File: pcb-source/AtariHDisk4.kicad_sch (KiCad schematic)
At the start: 19 parts, among them J1 JTAG, U4 Oscillator7x5, U9 5M80Z

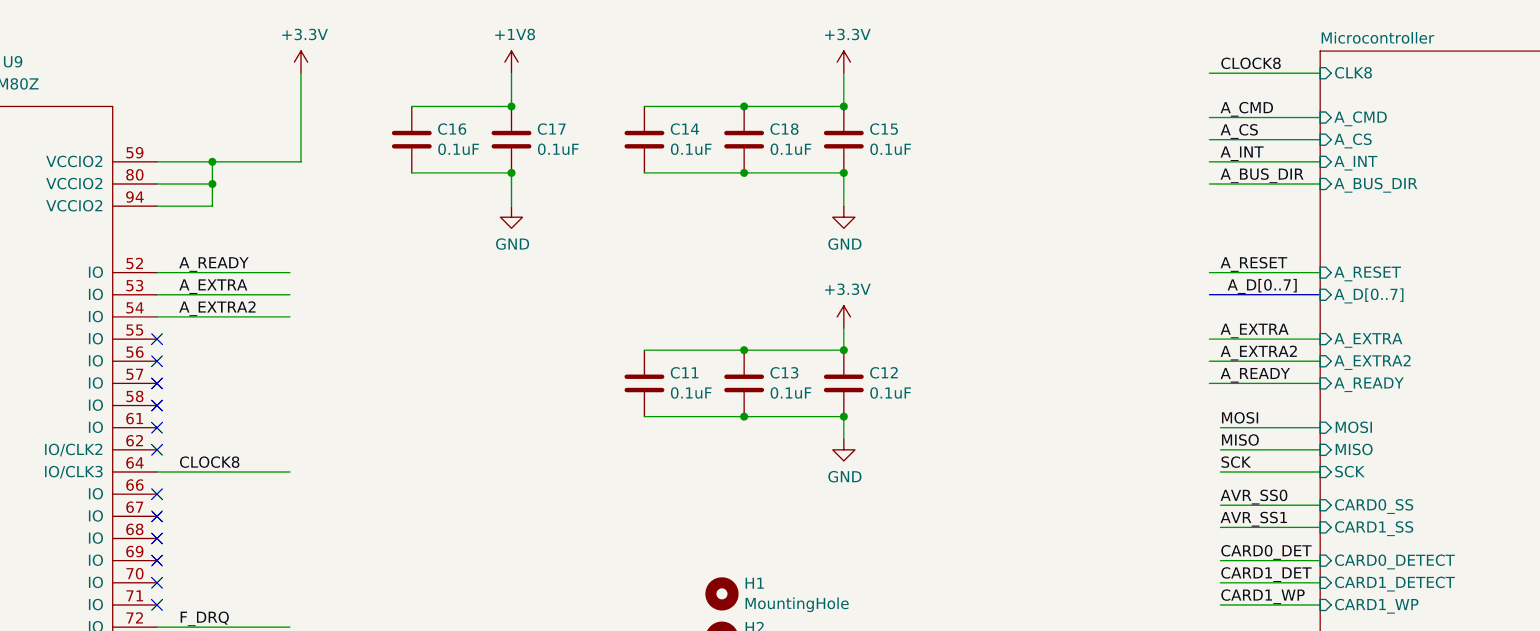
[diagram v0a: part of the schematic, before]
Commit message: Switched the avr128da to an stm32c031
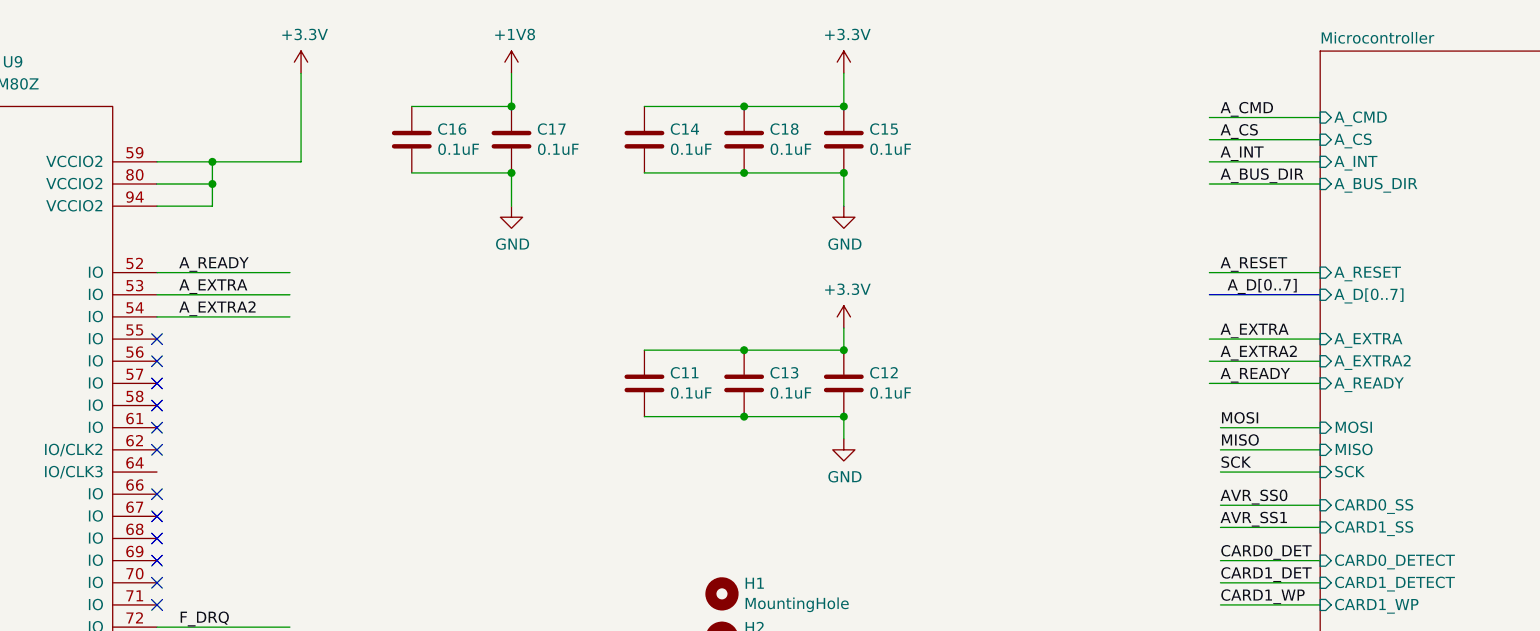
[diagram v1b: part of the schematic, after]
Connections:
- net CLOCK8: no longer names the net of U9.64 (IO/CLK3)
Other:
- sheet Microcontroller ports: added none; removed CLK8
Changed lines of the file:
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@@
-    (stroke (width 0) (type default))
-  )
-  (wire (pts (xy 104.14 73.66) (xy 119.38 73.66))
     (stroke (width 0) (type default))
   )
@@
     (stroke (width 0) (type default))
   )
-  (wire (pts (xy 224.79 27.94) (xy 237.49 27.94))
-    (stroke (width 0) (type default))
-  )
   (wire (pts (xy 104.14 147.32) (xy 119.38 147.32))
     (stroke (width 0) (type default))
@@
   )
   (label "A_READY" (at 226.06 63.5 0) (fields_autoplaced)
-    (effects (font (size 1.27 1.27)) (justify left bottom))
-  )
-  (label "CLOCK8" (at 226.06 27.94 0) (fields_autoplaced)
     (effects (font (size 1.27 1.27)) (justify left bottom))
   )
@@
   )
   (label "F_D[0..7]" (at 242.57 114.3 0) (fields_autoplaced)
-    (effects (font (size 1.27 1.27)) (justify left bottom))
-  )
-  (label "CLOCK8" (at 106.68 73.66 0) (fields_autoplaced)
     (effects (font (size 1.27 1.27)) (justify left bottom))
   )
@@
       (effects (font (size 1.27 1.27)) (justify left))
     )
-    (pin "CLK8" input (at 237.49 27.94 180)
-      (effects (font (size 1.27 1.27)) (justify left))
-    )

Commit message: Final board setup that was sent to production
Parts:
- added JP1: SolderJumper_2_Open, Jumper:SolderJumper-2_P1.3mm_Open_RoundedPad1.0x1.5mm, symbol Jumper:SolderJumper_2_Open
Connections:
- net A_BUS_DIR: now also U9.29 (IO); no longer U9.49 (IO)
- net A_CMD: now also U9.28 (IO); no longer U9.50 (IO)
- net A_CS: now also U9.34 (IO); no longer U9.48 (IO)
- net A_EXTRA: now also U9.26 (IO); no longer U9.53 (IO)
- net A_EXTRA2: now also U9.27 (IO); no longer U9.54 (IO)
- net A_INT: now also U9.49 (IO); no longer U9.51 (IO)
- net A_READY: now also U9.50 (IO); no longer U9.52 (IO)
- net CLK32: now also JP1.2 (B)
- net A_RESET: no longer names the net of U9.33 (IO)
- new net A_CLKOUT: JP1.1 (A)
- no-connect marks 49 -> 51
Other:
- sheet Microcontroller ports: added CLKOUT; removed none
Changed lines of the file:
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@@
   (no_connect (at 104.14 124.46))
   (no_connect (at 71.12 101.6))
+  (no_connect (at 104.14 55.88))
   (no_connect (at 104.14 119.38))
   (no_connect (at 104.14 60.96))
-  (no_connect (at 71.12 93.98))
+  (no_connect (at 71.12 104.14))
+  (no_connect (at 71.12 137.16))
   (no_connect (at 104.14 127))
   (no_connect (at 71.12 81.28))
   (no_connect (at 35.56 180.34))
+  (no_connect (at 104.14 58.42))
   (no_connect (at 104.14 83.82))
+  (no_connect (at 104.14 73.66))
   (no_connect (at 104.14 111.76))
   (no_connect (at 71.12 78.74))
-  (no_connect (at 104.14 58.42))
-  (no_connect (at 71.12 99.06))
   (no_connect (at 104.14 109.22))
   (no_connect (at 104.14 81.28))
   (no_connect (at 189.23 147.32))
   (no_connect (at 104.14 132.08))
-  (no_connect (at 71.12 96.52))
+  (no_connect (at 71.12 144.78))
   (no_connect (at 104.14 137.16))
   (no_connect (at 104.14 88.9))
   (no_connect (at 71.12 73.66))
+  (no_connect (at 104.14 53.34))
   (no_connect (at 104.14 78.74))
   (no_connect (at 104.14 76.2))
-  (no_connect (at 71.12 91.44))
   (no_connect (at 104.14 71.12))
-  (no_connect (at 71.12 106.68))
   (no_connect (at 71.12 134.62))
   (no_connect (at 104.14 134.62))
@@
   (no_connect (at 71.12 63.5))
   (no_connect (at 71.12 68.58))
+  (no_connect (at 104.14 50.8))
   (bus_entry (at 55.88 114.3) (size -2.54 2.54)
     (stroke (width 0) (type default))
@@
     (stroke (width 0) (type default))
   )
+  (wire (pts (xy 224.79 27.94) (xy 237.49 27.94))
+    (stroke (width 0) (type default))
+  )
   (bus (pts (xy 53.34 50.8) (xy 53.34 48.26))
     (stroke (width 0) (type default))
@@
     (stroke (width 0) (type default))
   )
-  (wire (pts (xy 104.14 50.8) (xy 119.38 50.8))
-    (stroke (width 0) (type default))
-  )
   (wire (pts (xy 180.34 156.21) (xy 226.06 156.21))
     (stroke (width 0) (type default))
@@
     (stroke (width 0) (type default))
   )
-  (wire (pts (xy 104.14 55.88) (xy 119.38 55.88))
-    (stroke (width 0) (type default))
-  )
   (wire (pts (xy 241.3 105.41) (xy 257.81 105.41))
     (stroke (width 0) (type default))
@@
     (stroke (width 0) (type default))
   )
+  (wire (pts (xy 55.88 93.98) (xy 71.12 93.98))
+    (stroke (width 0) (type default))
+  )
   (wire (pts (xy 104.14 165.1) (xy 110.49 165.1))
     (stroke (width 0) (type default))
@@
     (stroke (width 0) (type default))
   )
+  (wire (pts (xy 55.88 106.68) (xy 71.12 106.68))
+    (stroke (width 0) (type default))
+  )
   (bus (pts (xy 121.92 154.94) (xy 143.51 154.94))
     (stroke (width 0) (type default))
@@
     (stroke (width 0) (type default))
   )
+  (wire (pts (xy 55.88 91.44) (xy 71.12 91.44))
+    (stroke (width 0) (type default))
+  )
   (wire (pts (xy 35.56 175.26) (xy 35.56 177.8))
     (stroke (width 0) (type default))
@@
     (stroke (width 0) (type default))
   )
-  (wire (pts (xy 55.88 104.14) (xy 71.12 104.14))
-    (stroke (width 0) (type default))
-  )
   (wire (pts (xy 177.8 142.24) (xy 177.8 128.27))
     (stroke (width 0) (type default))
@@
     (stroke (width 0) (type default))
   )
+  (wire (pts (xy 55.88 99.06) (xy 71.12 99.06))
+    (stroke (width 0) (type default))
+  )
   (wire (pts (xy 241.3 102.87) (xy 257.81 102.87))
     (stroke (width 0) (type default))
@@
     (stroke (width 0) (type default))
   )
-  (wire (pts (xy 55.88 137.16) (xy 71.12 137.16))
-    (stroke (width 0) (type default))
-  )
   (wire (pts (xy 201.93 139.7) (xy 208.28 139.7))
     (stroke (width 0) (type default))
@@
     (stroke (width 0) (type default))
   )
+  (wire (pts (xy 33.02 71.12) (xy 48.26 71.12))
+    (stroke (width 0) (type default))
+  )
   (bus (pts (xy 121.92 142.24) (xy 121.92 144.78))
     (stroke (width 0) (type default))
@@
     (stroke (width 0) (type default))
   )
-  (wire (pts (xy 104.14 53.34) (xy 119.38 53.34))
-    (stroke (width 0) (type default))
-  )
   (wire (pts (xy 63.5 40.64) (xy 63.5 38.1))
     (stroke (width 0) (type default))
@@
     (stroke (width 0) (type default))
   )
+  (wire (pts (xy 55.88 96.52) (xy 71.12 96.52))
+    (stroke (width 0) (type default))
+  )
   (wire (pts (xy 182.88 43.18) (xy 182.88 39.37))
     (stroke (width 0) (type default))
@@
     (stroke (width 0) (type default))
   )
-  (wire (pts (xy 55.88 144.78) (xy 71.12 144.78))
-    (stroke (width 0) (type default))
-  )
   (wire (pts (xy 237.49 60.96) (xy 224.79 60.96))
     (stroke (width 0) (type default))
@@
     (effects (font (size 1.27 1.27)) (justify left bottom))
   )
-  (label "A_READY" (at 106.68 50.8 0) (fields_autoplaced)
+  (label "A_READY" (at 57.15 142.24 0) (fields_autoplaced)
     (effects (font (size 1.27 1.27)) (justify left bottom))
   )
@@
     (effects (font (size 1.27 1.27)) (justify left bottom))
   )
-  (label "A_EXTRA" (at 106.68 53.34 0) (fields_autoplaced)
+  (label "A_EXTRA" (at 57.15 91.44 0) (fields_autoplaced)
     (effects (font (size 1.27 1.27)) (justify left bottom))
   )
@@
     (effects (font (size 1.27 1.27)) (justify left bottom))
   )
-  (label "A_BUS_DIR" (at 57.15 139.7 0) (fields_autoplaced)
+  (label "A_BUS_DIR" (at 57.15 99.06 0) (fields_autoplaced)
     (effects (font (size 1.27 1.27)) (justify left bottom))
   )
@@
     (effects (font (size 1.27 1.27)) (justify left bottom))
   )
-  (label "A_RESET" (at 57.15 104.14 0) (fields_autoplaced)
-    (effects (font (size 1.27 1.27)) (justify left bottom))
-  )
   (label "TD0" (at 218.44 128.27 0) (fields_autoplaced)
     (effects (font (size 1.27 1.27)) (justify left bottom))
@@
     (effects (font (size 1.27 1.27)) (justify left bottom))
   )
-  (label "A_CMD" (at 57.15 142.24 0) (fields_autoplaced)
+  (label "A_CMD" (at 57.15 96.52 0) (fields_autoplaced)
     (effects (font (size 1.27 1.27)) (justify left bottom))
   )
@@
     (effects (font (size 1.27 1.27)) (justify left bottom))
   )
-  (label "A_INT" (at 57.15 144.78 0) (fields_autoplaced)
+  (label "A_INT" (at 57.15 139.7 0) (fields_autoplaced)
     (effects (font (size 1.27 1.27)) (justify left bottom))
   )
@@
     (effects (font (size 1.27 1.27)) (justify left bottom))
   )
-  (label "A_CS" (at 57.15 137.16 0) (fields_autoplaced)
+  (label "A_CS" (at 57.15 106.68 0) (fields_autoplaced)
     (effects (font (size 1.27 1.27)) (justify left bottom))
   )
@@
     (effects (font (size 1.27 1.27)) (justify left bottom))
   )
-  (label "A_RESET" (at 226.06 50.8 0) (fields_autoplaced)
+  (label "F_RESET" (at 226.06 50.8 0) (fields_autoplaced)
     (effects (font (size 1.27 1.27)) (justify left bottom))
   )
@@
     (effects (font (size 1.27 1.27)) (justify left bottom))
   )
+  (label "A_CLKOUT" (at 34.29 71.12 0) (fields_autoplaced)
+    (effects (font (size 1.27 1.27)) (justify left bottom))
+  )
   (label "F_D4" (at 106.68 149.86 0) (fields_autoplaced)
     (effects (font (size 1.27 1.27)) (justify left bottom))
@@
     (effects (font (size 1.27 1.27)) (justify right bottom))
   )
-  (label "A_EXTRA2" (at 106.68 55.88 0) (fields_autoplaced)
+  (label "A_EXTRA2" (at 57.15 93.98 0) (fields_autoplaced)
     (effects (font (size 1.27 1.27)) (justify left bottom))
   )
@@
   )
   (label "A_EXTRA2" (at 226.06 60.96 0) (fields_autoplaced)
+    (effects (font (size 1.27 1.27)) (justify left bottom))
+  )
+  (label "A_CLKOUT" (at 226.06 27.94 0) (fields_autoplaced)
     (effects (font (size 1.27 1.27)) (justify left bottom))
   )
@@
         (path "/b85bd53e-a419-4638-ac5c-9132c68f9083"
           (reference "#PWR057") (unit 1)
+        )
+      )
+    )
+  )
+  (symbol (lib_id "Jumper:SolderJumper_2_Open") (at 52.07 71.12 0) (unit 1)
+    (in_bom yes) (on_board yes) (dnp no) (fields_autoplaced)
+    (property "Reference" "JP1" (at 52.07 64.77 0)
+      (effects (font (size 1.27 1.27)))
+    )
+    (property "Value" "SolderJumper_2_Open" (at 52.07 67.31 0)
+      (effects (font (size 1.27 1.27)))
+    )
+    (property "Footprint" "Jumper:SolderJumper-2_P1.3mm_Open_RoundedPad1.0x1.5mm" (at 52.07 71.12 0)
+      (effects (font (size 1.27 1.27)) hide)
+    )
+    (property "Datasheet" "~" (at 52.07 71.12 0)
+      (effects (font (size 1.27 1.27)) hide)
+    )
+    (pin "2")
+    (pin "1")
+    (instances
+      (project "AtariHDisk4"
+        (path "/b85bd53e-a419-4638-ac5c-9132c68f9083"
+          (reference "JP1") (unit 1)
         )
       )
@@
       (effects (font (size 1.27 1.27)) (justify left))
     )
+    (pin "CLKOUT" input (at 237.49 27.94 180)
+      (effects (font (size 1.27 1.27)) (justify left))
+    )

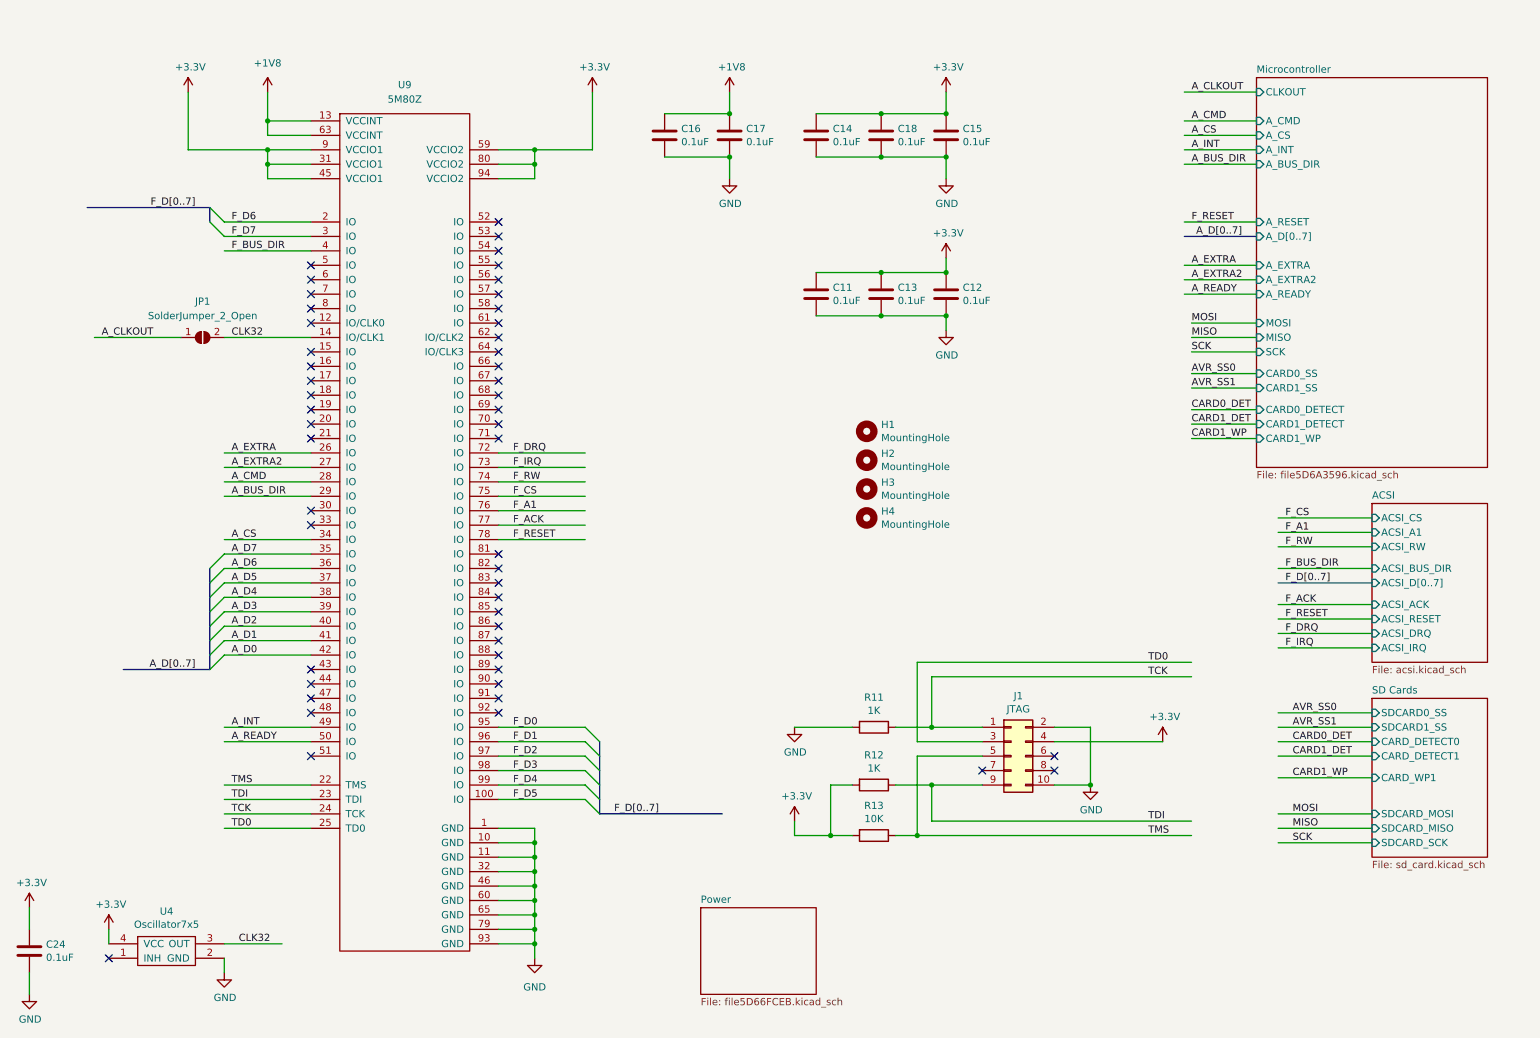
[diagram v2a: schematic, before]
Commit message: 1.2 version with 2 SPI buses
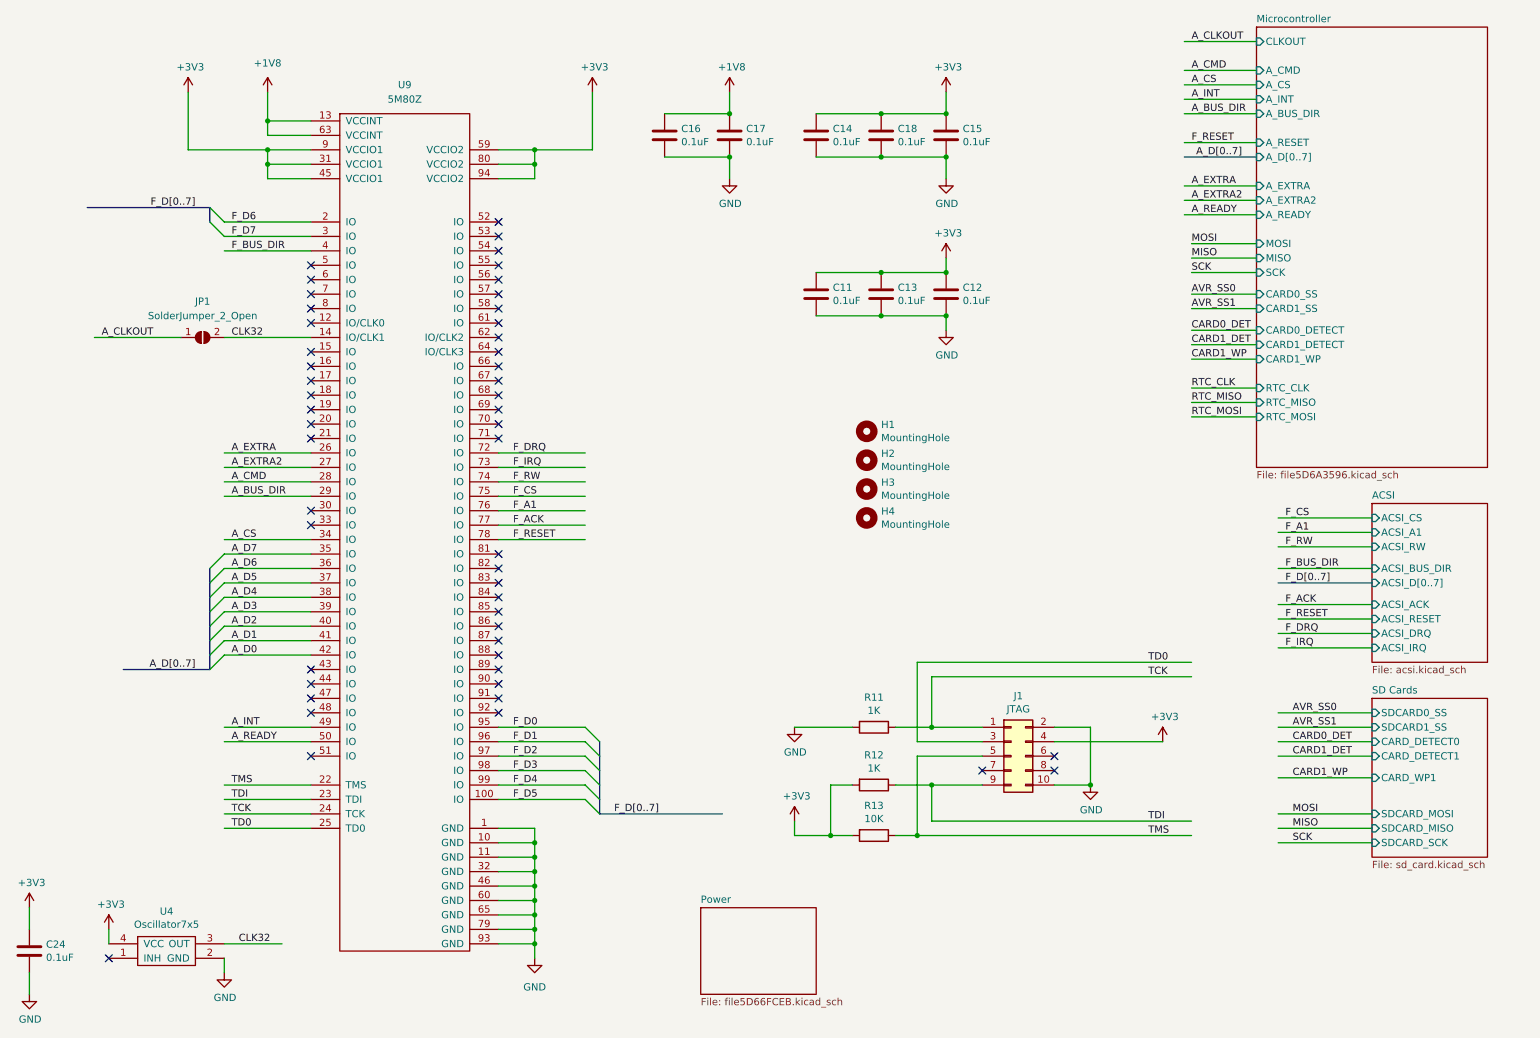
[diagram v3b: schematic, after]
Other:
- sheet Microcontroller ports: added RTC_CLK, RTC_MISO, RTC_MOSI; removed none
